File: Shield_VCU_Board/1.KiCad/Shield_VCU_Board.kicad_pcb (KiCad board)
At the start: 2 copper layers, 250.5 x 107.1 mm, 183 parts, among them J1 Conn_02x08_Odd_Even, J10 Main_Supply, J11 Conn_01x40_Socket, J13 Conn_Molex_TouchPanel, J14 CAN_OUT, J15 Conn_01x04_Socket, J16 CAN_IN, J2 Conn_02x10_Odd_Even, J3/1 NXP3, J4 Conn_02x08_Odd_Even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

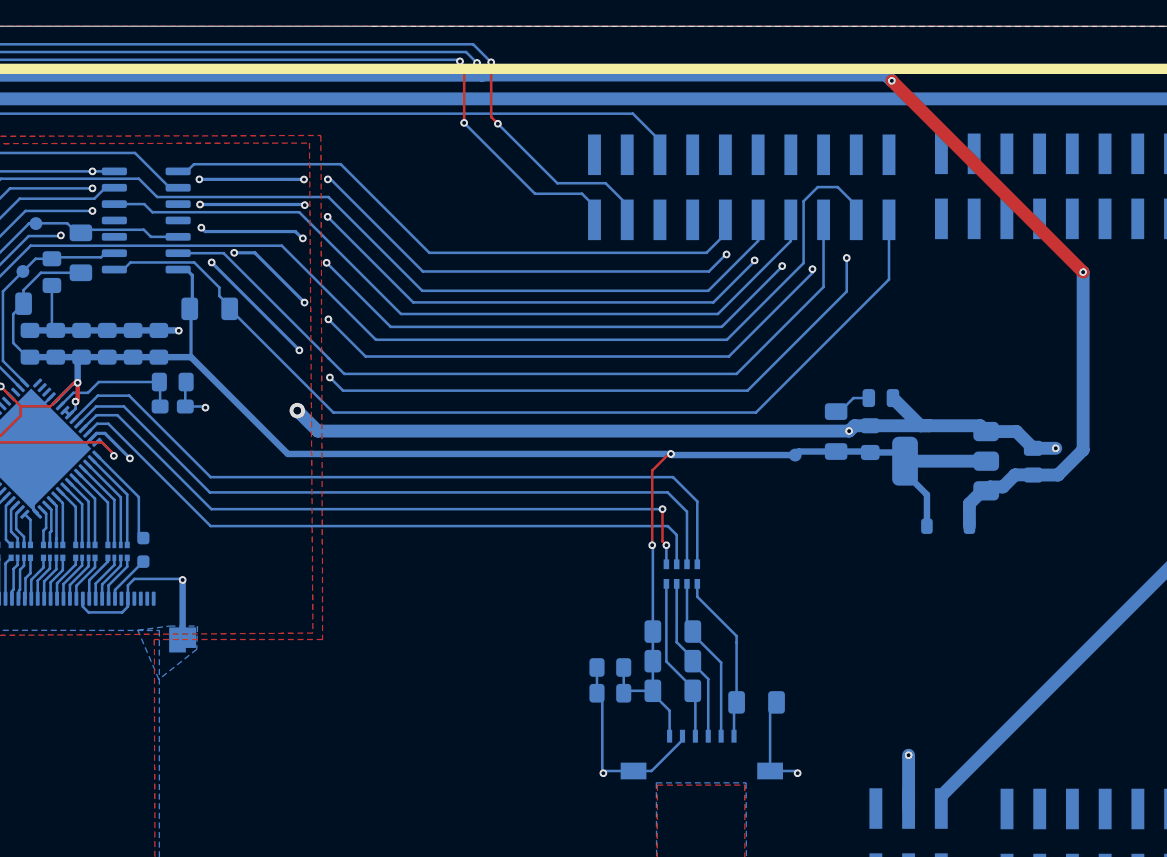
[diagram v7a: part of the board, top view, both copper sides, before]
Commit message: Changes to touchscreen i2c and display power
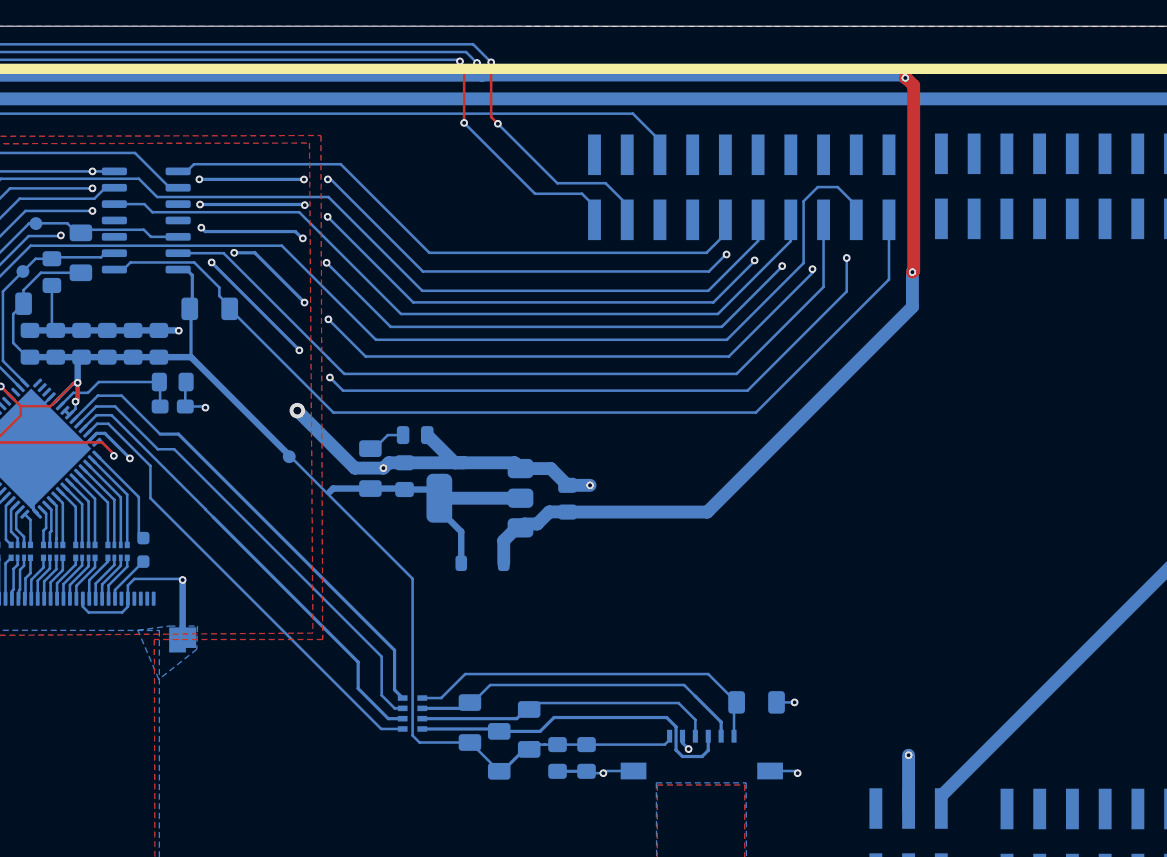
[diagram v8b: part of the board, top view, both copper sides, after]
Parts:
- moved DSPLV3.3 39.3 mm to (138.9, 77.4)
- moved D11 36.3 mm to (148.7, 75.7)
- moved C33 36.3 mm to (160.5, 80.7)
- moved C34 36.3 mm to (147.9, 78.9)
- moved D10 36.3 mm to (153.9, 85.7)
- moved R22 36.3 mm to (145.2, 78.3)
- moved U9 36.3 mm to (153.7, 80.6)
- moved RN8 23.5 mm to (148.5, 97.3), turned to 180 degrees
- moved R64 17.3 mm to (152.9, 98.0), turned to -90 degrees
- moved R63 15.2 mm to (155.2, 100.3), turned to -90 degrees
- moved R61 11.5 mm to (157.6, 98.6), turned to -90 degrees
- moved C16 8.13 mm to (159.8, 100.8), turned to -90 degrees
- moved C41 5.35 mm to (162.0, 100.8), turned to -90 degrees
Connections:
- RN8 pad 3: Net-(J13-Pin_4) -> Net-(J13-Pin_3)
- RN8 pad 4: Net-(J13-Pin_3) -> Net-(J13-Pin_4)
- U7 pad 25: Net-(RN8-R4.2) -> Net-(RN8-R3.2)
- U7 pad 26: Net-(RN8-R3.2) -> Net-(RN8-R4.2)
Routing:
- net GND: track 851.5 -> 804.0 mm, vias 75 -> 77
- net Net-(RN8-R1.2): track 57.4 -> 37.8 mm
- net 3V3_DSPL: track 172.8 -> 154.3 mm, vias 6 -> 4
- net Net-(RN8-R2.2): track 55.3 -> 37.2 mm
- net Net-(RN8-R4.2): track 52.8 -> 36.0 mm, vias 2 -> 0
- net Net-(RN8-R3.2): track 51.9 -> 36.2 mm
- net Net-(J13-Pin_6): track 13.2 -> 28.5 mm
- net Net-(J13-Pin_4): track 12.8 -> 26.7 mm
- net Net-(J13-Pin_5): track 12.9 -> 26.2 mm
- net +3.7V: track 246.7 -> 259.6 mm
- net Net-(J13-Pin_3): track 12.8 -> 24.0 mm
